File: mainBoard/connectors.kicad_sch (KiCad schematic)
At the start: 62 parts, among them J10 Conn_01x02, J11 Conn_02x05_Odd_Even, J12 Conn_01x02, J14 Conn_01x06, J17 Conn_01x05, J18 Conn_01x04, J19 Conn_01x14, J8 Conn_01x02, J9 Conn_01x02, Q3 IRLML6244TRPBF, Q4 IRLML6244TRPBF, Q5 IRLML6244TRPBF, Q8 PMOS, U17 SFH617A-2, U18 USBLC6-4SC6, U20 LM386, U21 USBLC6-4SC6, U23 USBLC6-4SC6, U24 USBLC6-2SC6, U26 100, U27 100, U28 100, U29 100, U30 74LVC1T45W6-7, U32 74LVC1T45W6-7

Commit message: working on layout
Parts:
- added D17: GRN, LED_SMD:LED_0603_1608Metric_Pad1.05x0.95mm_HandSolder, symbol Device:LED_Filled
- added H10, H9: MountingHole_Pad, MountingHole:MountingHole_3.2mm_M3_Pad_Via, symbol Mechanical:MountingHole_Pad
- added TP10, TP9: TestPoint_Small, TestPoint:TestPoint_Pad_D1.0mm, symbol Connector:TestPoint_Small
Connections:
- net GND: now also D17.1 (K), H10.1, H9.1
- net at J12.1 (Pin_1), U17.1: now also D17.2 (A)
- net at C52.2, U20.3 (+): now also TP10.1
- net at C47.1, C49.1, U20.5: now also TP9.1
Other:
- moved on the sheet: J12, R74, R78, U17

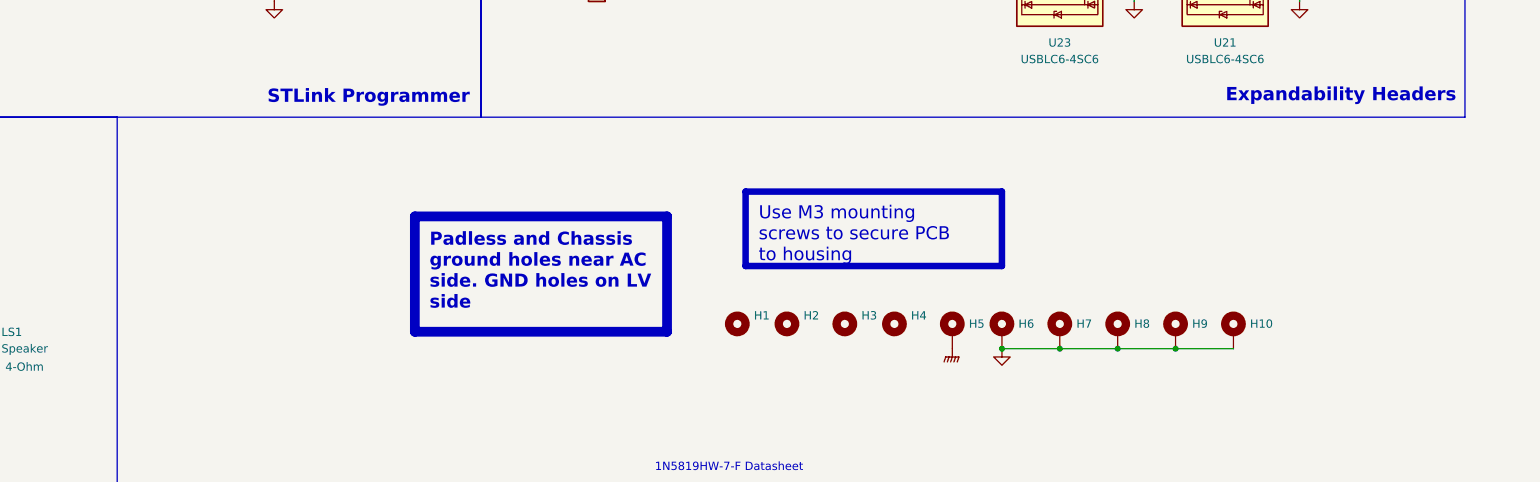
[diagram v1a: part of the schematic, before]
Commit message: add ws2812 led header
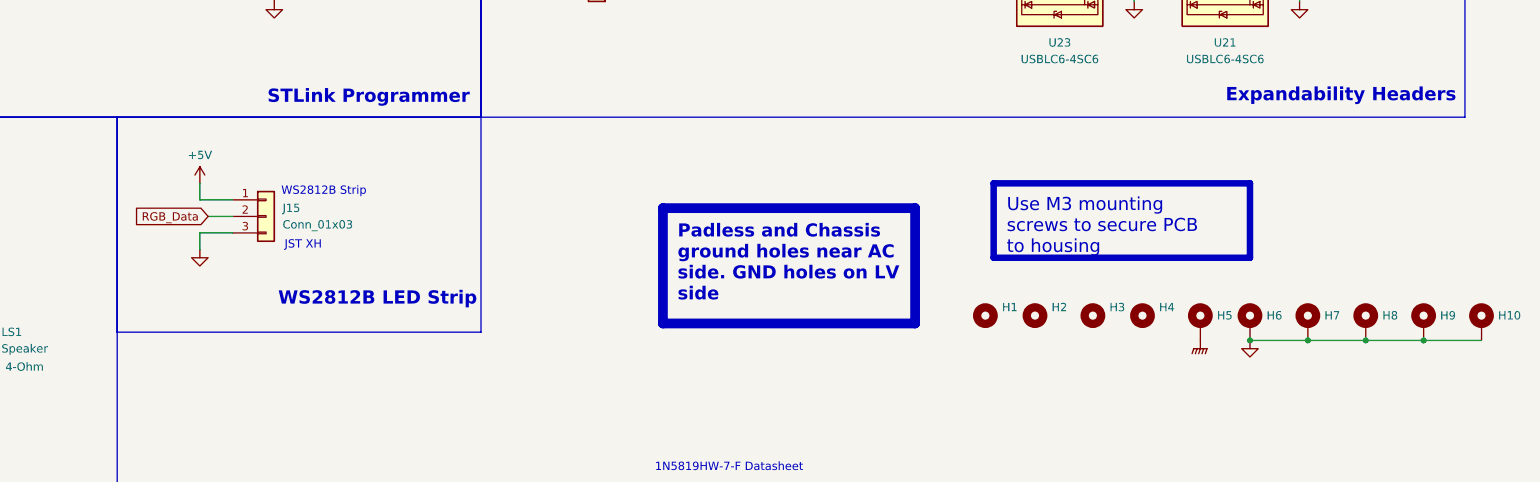
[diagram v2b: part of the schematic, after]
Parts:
- added J15: Conn_01x03, Connector_JST:JST_XH_B3B-XH-A_1x03_P2.50mm_Vertical, symbol Connector_Generic:Conn_01x03
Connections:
- net +5V: now also J15.1 (Pin_1)
- net GND: now also J15.3 (Pin_3)
- new net RGB_Data: J15.2 (Pin_2)
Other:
- note added: "WS2812B LED Strip"
- note added: "WS2812B Strip"
- moved on the sheet: H1, H10, H2, H3, H4, H5, H6, H7, H8, H9

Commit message: changes from windows copy to ubuntu
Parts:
- added C55: 100uF, Capacitor_SMD:C_Elec_6.3x5.8, symbol Device:C_Polarized
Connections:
- net +5V: now also C55.1
- net GND: now also C55.2
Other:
- moved on the sheet: J15

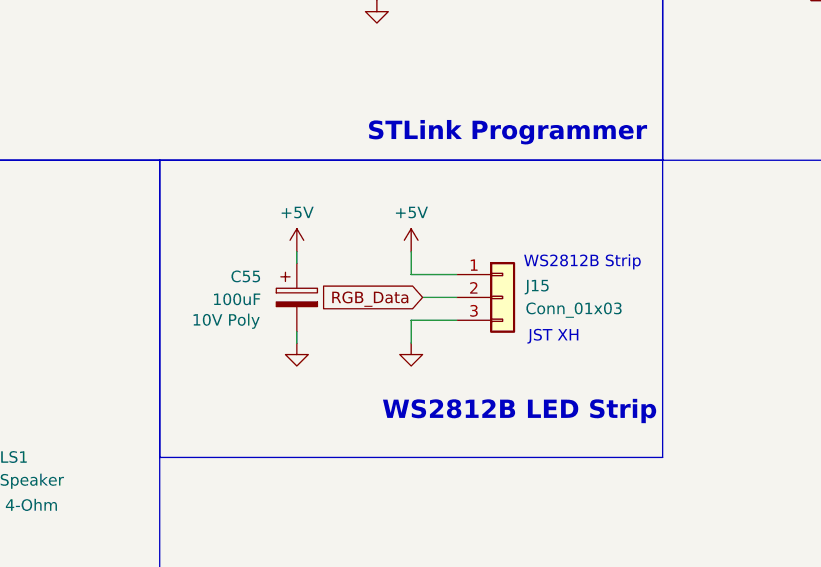
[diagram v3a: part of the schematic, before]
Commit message: change to 16MB ROM
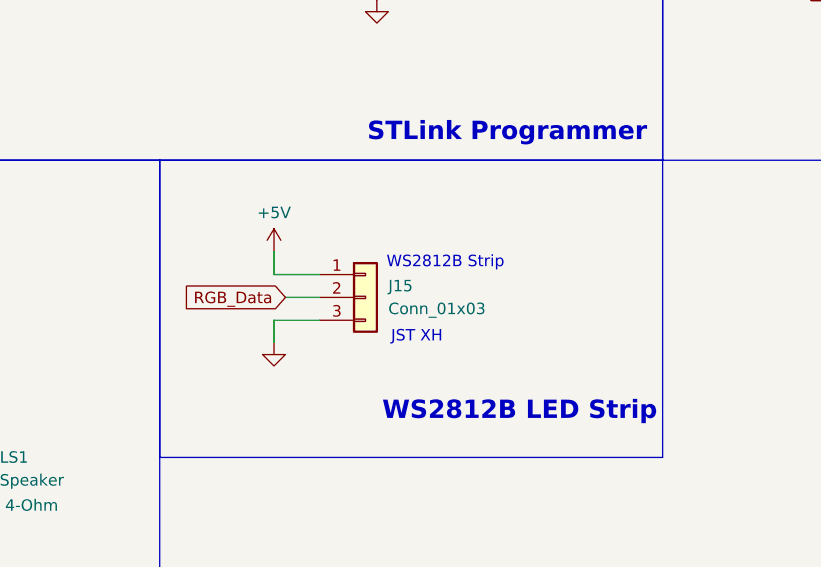
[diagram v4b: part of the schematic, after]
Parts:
- removed C55: 100uF, Capacitor_SMD:C_Elec_6.3x5.8, symbol Device:C_Polarized
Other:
- moved on the sheet: J15

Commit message: work on layout
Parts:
- added H11: MountingHole, MountingHole:MountingHole_3.2mm_M3, symbol Mechanical:MountingHole
- Q8: footprint (none) -> Package_TO_SOT_SMD:SOT-23
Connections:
- net LCD_BL: now also U29.8; no longer U29.2
- net SPI1_MOSI: now also U29.2; no longer U29.8
- net SPI1_SCK: now also U28.2, U28.6; no longer U28.4, U28.8
- net Touch_CS: now also U28.8; no longer U28.2
- net at U28.1: now also J19.7 (Pin_7); no longer J19.11 (Pin_11)
- net at U28.3: now also J19.9 (Pin_9); no longer J19.10 (Pin_10)
- net at U28.5: now also J19.10 (Pin_10); no longer J19.9 (Pin_9)
- net at U28.7: now also J19.11 (Pin_11); no longer J19.7 (Pin_7)
- net at Q8.2 (G), R84.1: now also U29.7; no longer U29.1
- net at U29.3: now also J19.13 (Pin_13); no longer J19.14 (Pin_14)
- net at U29.4: now also U28.4, U30.4 (B); no longer U32.4 (B)
- net at U29.5: now also J19.14 (Pin_14); no longer J19.13 (Pin_13)
- net at J19.12 (Pin_12): now also U29.1; no longer U29.7
- new net: U29.6, U32.4 (B)
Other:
- moved on the sheet: U28, U29
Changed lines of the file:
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@@
 	(symbol
 		(lib_id "Parallel_Resistor:ParallelArray-4")
-		(at 330.2 81.28 180)
+		(at 330.2 91.44 0)
+		(mirror y)
 		(unit 1)
 		(body_style 1)
@@
 		(dnp no)
 		(property "Reference" "U28"
-			(at 329.438 95.504 0)
+			(at 329.438 93.472 0)
 			(show_name no)
 			(do_not_autoplace no)
@@
 		)
 		(property "Value" "100"
-			(at 329.438 93.472 0)
+			(at 329.438 95.504 0)
 			(show_name no)
 			(do_not_autoplace no)
@@
 		)
 		(property "Footprint" "Resistor_SMD:R_Array_Convex_4x1206"
-			(at 330.2 81.28 0)
+			(at 330.2 91.44 0)
 			(hide yes)
 			(show_name no)
@@
 		)
 		(property "Datasheet" ""
-			(at 330.2 81.28 0)
+			(at 330.2 91.44 0)
 			(hide yes)
 			(show_name no)
@@
 		)
 		(property "Description" ""
-			(at 330.2 81.28 0)
+			(at 330.2 91.44 0)
 			(hide yes)
 			(show_name no)
@@
 		)
 		(property "part number" "RAVF164DJT100R"
-			(at 330.2 81.28 0)
+			(at 330.2 91.44 0)
 			(hide yes)
 			(show_name no)
@@
 	(symbol
 		(lib_id "Parallel_Resistor:ParallelArray-4")
-		(at 330.2 97.79 180)
+		(at 330.2 107.95 0)
+		(mirror y)
 		(unit 1)
 		(body_style 1)
@@
 		(dnp no)
 		(property "Reference" "U29"
-			(at 329.438 112.014 0)
+			(at 329.438 110.236 0)
 			(show_name no)
 			(do_not_autoplace no)
@@
 		)
 		(property "Value" "100"
-			(at 329.438 109.982 0)
+			(at 329.438 112.268 0)
 			(show_name no)
 			(do_not_autoplace no)
@@
 		)
 		(property "Footprint" "Resistor_SMD:R_Array_Convex_4x1206"
-			(at 330.2 97.79 0)
+			(at 330.2 107.95 0)
 			(hide yes)
 			(show_name no)
@@
 		)
 		(property "Datasheet" ""
-			(at 330.2 97.79 0)
+			(at 330.2 107.95 0)
 			(hide yes)
 			(show_name no)
@@
 		)
 		(property "Description" ""
-			(at 330.2 97.79 0)
+			(at 330.2 107.95 0)
 			(hide yes)
 			(show_name no)
@@
 		)
 		(property "part number" "RAVF164DJT100R"
-			(at 330.2 97.79 0)
+			(at 330.2 107.95 0)
 			(hide yes)
 			(show_name no)
@@
 	)
 	(symbol
+		(lib_id "Mechanical:MountingHole")
+		(at 335.28 237.49 0)
+		(unit 1)
+		(body_style 1)
+		(exclude_from_sim no)
+		(in_bom no)
+		(on_board yes)
+		(in_pos_files yes)
+		(dnp no)
+		(fields_autoplaced yes)
+		(property "Reference" "H11"
+			(at 337.82 236.22 0)
+			(show_name no)
+			(do_not_autoplace no)
+			(effects
+				(font
+					(size 1.27 1.27)
+				)
+				(justify left)
+			)
+		)
+		(property "Value" "MountingHole"
+			(at 337.82 238.76 0)
+			(hide yes)
+			(show_name no)
+			(do_not_autoplace no)
+			(effects
+				(font
+					(size 1.27 1.27)
+				)
+				(justify left)
+			)
+		)
+		(property "Footprint" "MountingHole:MountingHole_3.2mm_M3"
+			(at 335.28 237.49 0)
+			(hide yes)
+			(show_name no)
+			(do_not_autoplace no)
+			(effects
+				(font
+					(size 1.27 1.27)
+				)
+			)
+		)
+		(property "Datasheet" ""
+			(at 335.28 237.49 0)
+			(hide yes)
+			(show_name no)
+			(do_not_autoplace no)
+			(effects
+				(font
+					(size 1.27 1.27)
+				)
+			)
+		)
+		(property "Description" "Mounting Hole without connection"
+			(at 335.28 237.49 0)
+			(hide yes)
+			(show_name no)
+			(do_not_autoplace no)
+			(effects
+				(font
+					(size 1.27 1.27)
+				)
+			)
+		)
+		(instances
+			(project "mainBoard"
+				(path "/0650c7a8-acba-429c-9f8e-eec0baf0bc1c/fede4c36-00cc-4d3d-b71c-5243ba232202/be0cd71a-2de9-4b13-b090-17b54a3e018c"
+					(reference "H11")
+					(unit 1)
+				)
+			)
+		)
+	)
+	(symbol
 		(lib_id "power:GND")
 		(at 88.9 222.25 0)
@@
 			)
 		)
-		(property "Footprint" ""
+		(property "Footprint" "Package_TO_SOT_SMD:SOT-23"
 			(at 361.95 119.38 0)
 			(hide yes)

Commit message: work on layout
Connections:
- net ESD_PB12: now also U23.3 (I/O2), U26.7; no longer U23.1 (I/O1), U26.1
- net ESD_PB13: now also U23.1 (I/O1), U26.5; no longer U23.3 (I/O2), U26.3
- net ESD_PB14: now also U23.6 (I/O4), U26.3; no longer U23.4 (I/O3), U26.5
- net ESD_PB15: now also U23.4 (I/O3), U26.1; no longer U23.6 (I/O4), U26.7
- net PB12: now also U26.8; no longer U26.2
- net PB13: now also U26.6; no longer U26.4
- net PB14: now also U26.4; no longer U26.6
- net PB15: now also U26.2; no longer U26.8
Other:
- moved on the sheet: U26
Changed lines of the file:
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@@
 	)
 	(junction
+		(at 328.93 168.91)
+		(diameter 0)
+		(color 0 0 0 0)
+	)
+	(junction
 		(at 157.48 138.43)
 		(diameter 0)
@@
 	)
 	(junction
-		(at 328.93 166.37)
-		(diameter 0)
-		(color 0 0 0 0)
-	)
-	(junction
 		(at 107.95 233.68)
 		(diameter 0)
@@
 	)
 	(junction
-		(at 123.19 233.68)
+		(at 331.47 161.29)
 		(diameter 0)
 		(color 0 0 0 0)
 	)
 	(junction
-		(at 64.77 265.43)
+		(at 123.19 233.68)
 		(diameter 0)
 		(color 0 0 0 0)
 	)
 	(junction
-		(at 88.9 243.84)
+		(at 326.39 166.37)
 		(diameter 0)
 		(color 0 0 0 0)
 	)
 	(junction
-		(at 359.41 113.03)
+		(at 64.77 265.43)
 		(diameter 0)
 		(color 0 0 0 0)
 	)
 	(junction
-		(at 326.39 168.91)
+		(at 88.9 243.84)
 		(diameter 0)
 		(color 0 0 0 0)
 	)
 	(junction
-		(at 77.47 138.43)
+		(at 359.41 113.03)
 		(diameter 0)
 		(color 0 0 0 0)
 	)
 	(junction
-		(at 77.47 63.5)
+		(at 334.01 163.83)
 		(diameter 0)
 		(color 0 0 0 0)
 	)
 	(junction
-		(at 331.47 163.83)
+		(at 77.47 138.43)
 		(diameter 0)
 		(color 0 0 0 0)
 	)
 	(junction
-		(at 334.01 161.29)
+		(at 77.47 63.5)
 		(diameter 0)
 		(color 0 0 0 0)
@@
 	(wire
 		(pts
-			(xy 331.47 163.83) (xy 316.23 163.83)
+			(xy 316.23 163.83) (xy 334.01 163.83)
 		)
 		(stroke
@@
 	(wire
 		(pts
-			(xy 334.01 161.29) (xy 334.01 173.99)
-		)
-		(stroke
-			(width 0)
-			(type default)
-		)
-	)
-	(wire
-		(pts
-			(xy 326.39 168.91) (xy 316.23 168.91)
+			(xy 316.23 168.91) (xy 328.93 168.91)
 		)
 		(stroke
@@
 	(wire
 		(pts
-			(xy 334.01 161.29) (xy 316.23 161.29)
-		)
-		(stroke
-			(width 0)
-			(type default)
-		)
-	)
-	(wire
-		(pts
 			(xy 147.32 62.23) (xy 166.37 62.23)
 		)
@@
 	(wire
 		(pts
-			(xy 331.47 173.99) (xy 331.47 163.83)
-		)
-		(stroke
-			(width 0)
-			(type default)
-		)
-	)
-	(wire
-		(pts
 			(xy 292.1 158.75) (xy 297.18 158.75)
 		)
@@
 	(wire
 		(pts
-			(xy 328.93 166.37) (xy 328.93 173.99)
-		)
-		(stroke
-			(width 0)
-			(type default)
-		)
-	)
-	(wire
-		(pts
 			(xy 276.86 53.34) (xy 276.86 55.88)
 		)
@@
 	(wire
 		(pts
-			(xy 134.62 129.54) (xy 134.62 132.08)
+			(xy 328.93 168.91) (xy 363.22 168.91)
 		)
 		(stroke
@@
 	(wire
 		(pts
-			(xy 334.01 87.63) (xy 354.33 87.63)
+			(xy 134.62 129.54) (xy 134.62 132.08)
 		)
 		(stroke
@@
 	(wire
 		(pts
-			(xy 363.22 166.37) (xy 328.93 166.37)
+			(xy 334.01 87.63) (xy 354.33 87.63)
 		)
 		(stroke
@@
 	(wire
 		(pts
+			(xy 331.47 161.29) (xy 331.47 173.99)
+		)
+		(stroke
+			(width 0)
+			(type default)
+		)
+	)
+	(wire
+		(pts
 			(xy 199.39 62.23) (xy 199.39 66.04)
 		)
@@
 	(wire
 		(pts
-			(xy 363.22 161.29) (xy 334.01 161.29)
+			(xy 326.39 166.37) (xy 363.22 166.37)
+		)
+		(stroke
+			(width 0)
+			(type default)
+		)
+	)
+	(wire
+		(pts
+			(xy 331.47 161.29) (xy 363.22 161.29)
 		)
 		(stroke
@@
 	(wire
 		(pts
+			(xy 331.47 161.29) (xy 316.23 161.29)
+		)
+		(stroke
+			(width 0)
+			(type default)
+		)
+	)
+	(wire
+		(pts
 			(xy 146.05 177.8) (xy 156.21 177.8)
 		)
@@
 	(wire
 		(pts
+			(xy 326.39 166.37) (xy 326.39 173.99)
+		)
+		(stroke
+			(width 0)
+			(type default)
+		)
+	)
+	(wire
+		(pts
 			(xy 170.18 121.92) (xy 171.45 121.92)
 		)
@@
 	(wire
 		(pts
+			(xy 328.93 168.91) (xy 328.93 173.99)
+		)
+		(stroke
+			(width 0)
+			(type default)
+		)
+	)
+	(wire
+		(pts
 			(xy 81.28 231.14) (xy 91.44 231.14)
 		)
@@
 	(wire
 		(pts
+			(xy 334.01 163.83) (xy 334.01 173.99)
+		)
+		(stroke
+			(width 0)
+			(type default)
+		)
+	)
+	(wire
+		(pts
 			(xy 77.47 48.26) (xy 77.47 49.53)
 		)
@@
 	(wire
 		(pts
-			(xy 328.93 166.37) (xy 316.23 166.37)
+			(xy 316.23 166.37) (xy 326.39 166.37)
 		)
 		(stroke
@@
 	(wire
 		(pts
-			(xy 77.47 77.47) (xy 77.47 85.09)
+			(xy 334.01 163.83) (xy 363.22 163.83)
 		)
 		(stroke
@@
 	(wire
 		(pts
-			(xy 80.01 58.42) (xy 77.47 58.42)
-		)
-		(stroke
-			(width 0)
-			(type default)
-		)
-	)
-	(wire
-		(pts
-			(xy 377.19 234.95) (xy 386.08 234.95)
+			(xy 77.47 77.47) (xy 77.47 85.09)
 		)
 		(stroke
@@
 	(wire
 		(pts
-			(xy 77.47 102.87) (xy 77.47 109.22)
+			(xy 80.01 58.42) (xy 77.47 58.42)
 		)
 		(stroke
@@
 	(wire
 		(pts
-			(xy 336.55 82.55) (xy 334.01 82.55)
+			(xy 377.19 234.95) (xy 386.08 234.95)
 		)
 		(stroke
@@
 	(wire
 		(pts
-			(xy 363.22 168.91) (xy 326.39 168.91)
+			(xy 77.47 102.87) (xy 77.47 109.22)
 		)
 		(stroke
@@
 	(wire
 		(pts
-			(xy 326.39 168.91) (xy 326.39 173.99)
+			(xy 336.55 82.55) (xy 334.01 82.55)
 		)
 		(stroke
@@
 	(wire
 		(pts
-			(xy 363.22 163.83) (xy 331.47 163.83)
-		)
-		(stroke
-			(width 0)
-			(type default)
-		)
-	)
-	(wire
-		(pts
 			(xy 71.12 157.48) (xy 71.12 153.67)
 		)
@@
 		(shape bidirectional)
 		(at 292.1 168.91 180)
-		(fields_autoplaced yes)
 		(effects
 			(font
@@
 		)
 		(property "Intersheetrefs" "${INTERSHEET_REFS}"
-			(at 283.0445 168.91 0)
+			(at 291.9345 163.83 0)
 			(hide yes)
 			(show_name no)
@@
 		(shape bidirectional)
 		(at 292.1 166.37 180)
-		(fields_autoplaced yes)
 		(effects
 			(font
@@
 		)
 		(property "Intersheetrefs" "${INTERSHEET_REFS}"
-			(at 283.0445 166.37 0)
+			(at 291.9345 161.29 0)
 			(hide yes)
 			(show_name no)
@@
 	(symbol
 		(lib_id "Parallel_Resistor:ParallelArray-4")
-		(at 312.42 160.02 180)
+		(at 312.42 170.18 0)
+		(mirror y)
 		(unit 1)
 		(body_style 1)
@@
 		(dnp no)
 		(property "Reference" "U26"
-			(at 311.658 174.244 0)
+			(at 311.912 172.72 0)
 			(show_name no)
 			(do_not_autoplace no)
@@
 		)
 		(property "Value" "100"
-			(at 311.658 172.212 0)
+			(at 311.912 174.752 0)
 			(show_name no)
 			(do_not_autoplace no)
@@
 		)
 		(property "Footprint" "Resistor_SMD:R_Array_Convex_4x1206"
-			(at 312.42 160.02 0)
+			(at 312.42 170.18 0)
 			(hide yes)
 			(show_name no)
@@
 		)
 		(property "Datasheet" ""
-			(at 312.42 160.02 0)
+			(at 312.42 170.18 0)
 			(hide yes)
 			(show_name no)
@@
 		)
 		(property "Description" ""
-			(at 312.42 160.02 0)
+			(at 312.42 170.18 0)
 			(hide yes)
 			(show_name no)
@@
 		)
 		(property "part number" "RAVF164DJT100R"
-			(at 312.42 160.02 0)
+			(at 312.42 170.18 0)
 			(hide yes)
 			(show_name no)

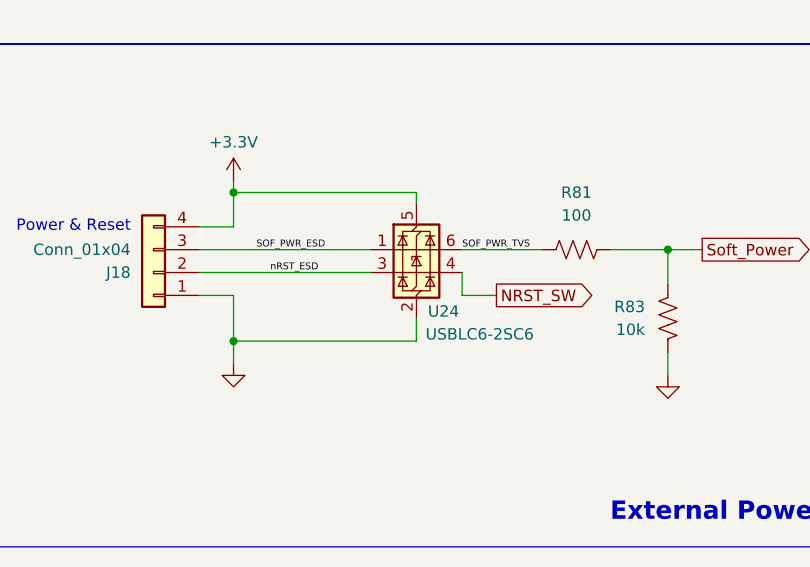
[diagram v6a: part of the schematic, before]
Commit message: remove dual ESD protection on nRST and route nrst to stlink
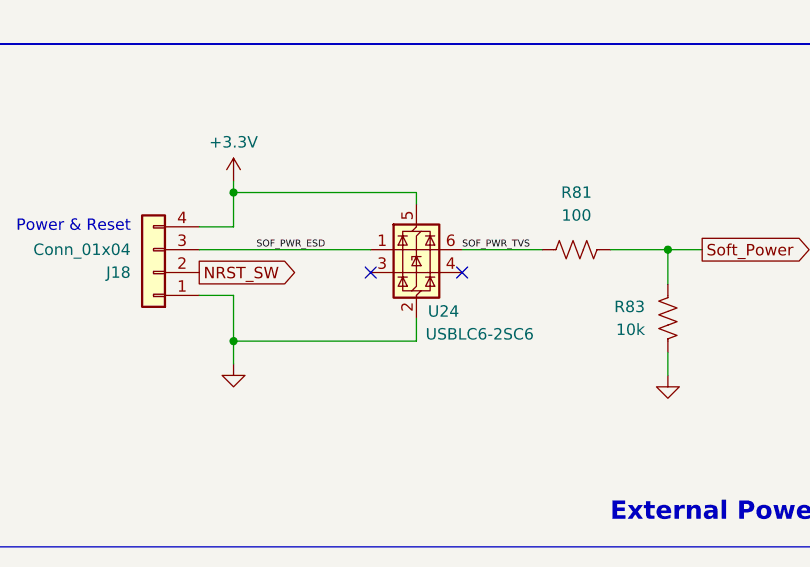
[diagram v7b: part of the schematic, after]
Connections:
- net NRST_SW: now also J18.2 (Pin_2); no longer U24.4 (I/O2)
- net nRST_ESD: no longer names the net of U24.3 (I/O2)
- net nRST_ESD: no longer J18.2 (Pin_2)
- no-connect marks 5 -> 7
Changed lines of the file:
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@@
+	)
+	(no_connect
+		(at 166.37 64.77)
 	)
 	(no_connect
@@
 		(at 201.93 177.8)
 	)
+	(no_connect
+		(at 176.53 64.77)
+	)
 	(wire
 		(pts
@@
 	(wire
 		(pts
-			(xy 147.32 64.77) (xy 166.37 64.77)
-		)
-		(stroke
-			(width 0)
-			(type default)
-		)
-	)
-	(wire
-		(pts
 			(xy 151.13 72.39) (xy 171.45 72.39)
 		)
@@
 	(wire
 		(pts
-			(xy 176.53 67.31) (xy 180.34 67.31)
-		)
-		(stroke
-			(width 0)
-			(type default)
-		)
-	)
-	(wire
-		(pts
 			(xy 114.3 245.11) (xy 114.3 255.27)
 		)
@@
 		(pts
 			(xy 334.01 72.39) (xy 354.33 72.39)
-		)
-		(stroke
-			(width 0)
-			(type default)
-		)
-	)
-	(wire
-		(pts
-			(xy 176.53 67.31) (xy 176.53 64.77)
 		)
 		(stroke
@@
 	(label "FAN1_MINUS"
 		(at 77.47 66.04 0)
-		(effects
-			(font
-				(size 0.762 0.762)
-			)
-			(justify left bottom)
-		)
-	)
-	(label "nRST_ESD"
-		(at 155.2163 64.77 0)
 		(effects
 			(font
@@
 	(global_label "NRST_SW"
 		(shape output)
-		(at 180.34 67.31 0)
+		(at 147.32 64.77 0)
 		(fields_autoplaced yes)
 		(effects
@@
 		)
 		(property "Intersheetrefs" "${INTERSHEET_REFS}"
-			(at 191.7313 67.31 0)
+			(at 158.7113 64.77 0)
 			(hide yes)
 			(show_name no)
